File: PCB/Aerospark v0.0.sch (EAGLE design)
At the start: 15 parts, among them T1 2N3904

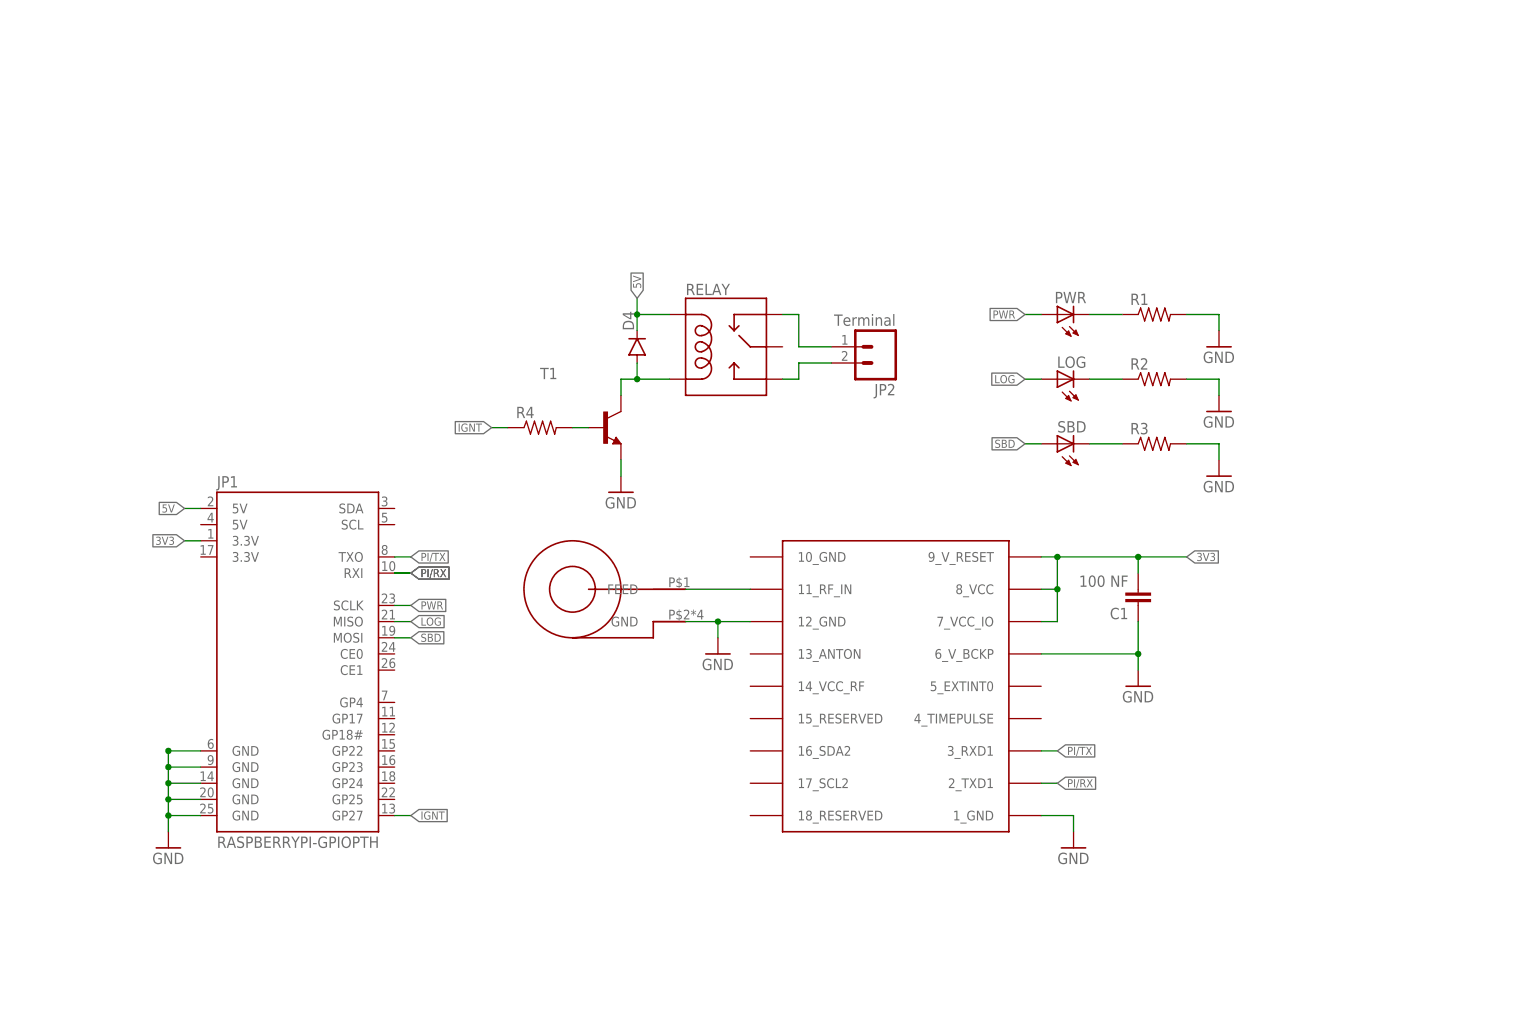
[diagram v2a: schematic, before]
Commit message: Updated PCB to optoisolator & darlington drivers
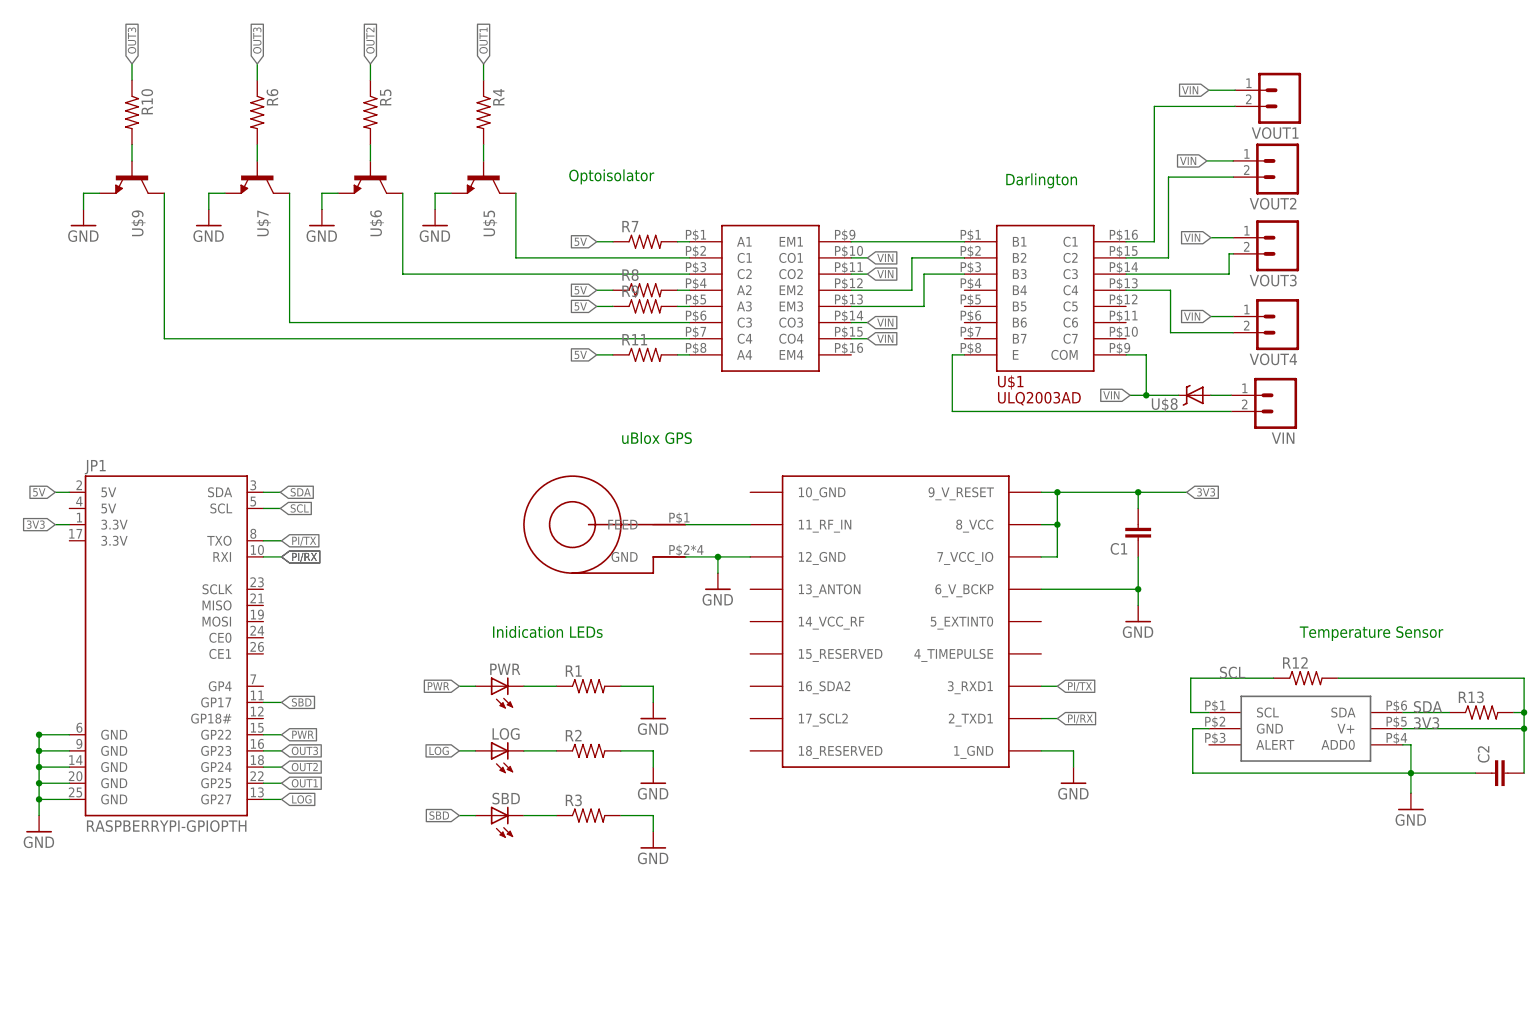
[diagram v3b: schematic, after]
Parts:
- removed D4: (no value), SparkFun-DiscreteSemi:DIODESMB
- removed JP2: Terminal, SparkFun-Connectors:M023.5MM_LOCK
- removed RELAY: RELAYPTH3, SparkFun-Electromechanical:RELAYPTH3
- removed T1: 2N3904, transistor:2N3904
- added C2: (no value), SparkFun-Capacitors:CAP0805
- added R10, R11, R12, R13, R5, R6, R7, R8, R9: (no value), resistor:R-US_R0805
- added U$1: ULQ2003A, ULQ2003AD:ULQ2003A
- added U$10: TMP102, TMP102:TMP102
- added U$4: ILQ2-X009, ILQ2-X009:ILQ2-X009
- added U$5, U$6, U$7, U$9: MMBT3904FSCT-ND, GuShH:MMBT3904FSCT-ND
- added U$8: VISHAY_SCHOTTKY, Ava:VISHAY_SCHOTTKY
- added VIN, VOUT1, VOUT2, VOUT3, VOUT4: M023.5MM_LOCK, SparkFun-Connectors:M023.5MM_LOCK
- C1: value 100 NF -> (none)
- R4: MF SLI (CML/IDI) -> (none); MPN CMD17-21VGD/TR8 -> (none); OC_NEWARK 34C8662 -> (none)
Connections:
- removed net IGNT: JP1.GP27, R4.1
- new net N$10: U$4.C1, U$5.C
- new net N$12: U$4.C2, U$6.C
- new net N$13: U$4.C3, U$7.C
- new net N$14: U$1.E, VIN.2
- new net N$15: R4.2, U$5.B
- new net N$16: R5.2, U$6.B
- new net N$17: R6.2, U$7.B
- new net N$18: U$8.A, VIN.1
- new net N$20: U$1.C2, VOUT2.2
- new net N$21: U$1.C3, VOUT3.2
- new net N$22: U$1.C4, VOUT4.2
- new net N$24: U$1.B1, U$4.EM1
- new net N$25: U$1.B2, U$4.EM2
- new net N$26: U$1.B3, U$4.EM3
- new net N$27: R10.2, U$9.B
- new net N$28: U$4.C4, U$9.C
- new net N$29: R11.2, U$4.A4
- new net OUT1: JP1.GP25, R4.1
- new net OUT2: JP1.GP24, R5.1
- new net OUT3: JP1.GP23, R10.1, R6.1
- new net SCL: JP1.SCL, R12.1, U$10.SCL
- new net SDA: JP1.SDA, R13.1, U$10.SDA
- new net VIN: U$1.COM, U$4.CO1, U$4.CO2, U$4.CO3, U$4.CO4, U$8.C, VOUT1.1, VOUT2.1, VOUT3.1, VOUT4.1
- net 3V3: now also C2.2, R12.2, R13.2, U$10.V+
- net 5V: now also R11.1, R7.1, R8.1, R9.1; no longer D4.C, RELAY.COIL1
- net GND: now also C2.1, U$10.ADD0, U$10.GND, U$5.E, U$6.E, U$7.E, U$9.E; no longer T1.E
- net LOG: now also JP1.GP27; no longer JP1.MISO
- net N$2: now also R7.2, U$4.A1; no longer JP2.1, RELAY.NC
- net N$6: now also R8.2, U$4.A2; no longer R4.2, T1.B
- net N$7: now also R9.2, U$4.A3; no longer JP2.2, RELAY.NO
- net N$8: now also U$1.C1, VOUT1.2; no longer D4.A, RELAY.COIL2, T1.C
- net PWR: now also JP1.GP22; no longer JP1.SCLK
- net SBD: now also JP1.GP17; no longer JP1.MOSI
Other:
- note added: "Darlington"
- note added: "Inidication LEDs"
- note added: "Optoisolator"
- note added: "Temperature Sensor"
- note added: "uBlox GPS"
- moved on the sheet: C1, JP1, LOG, PWR, R1, R2, R3, R4, SBD

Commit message: Updated PCB and added mounting hole
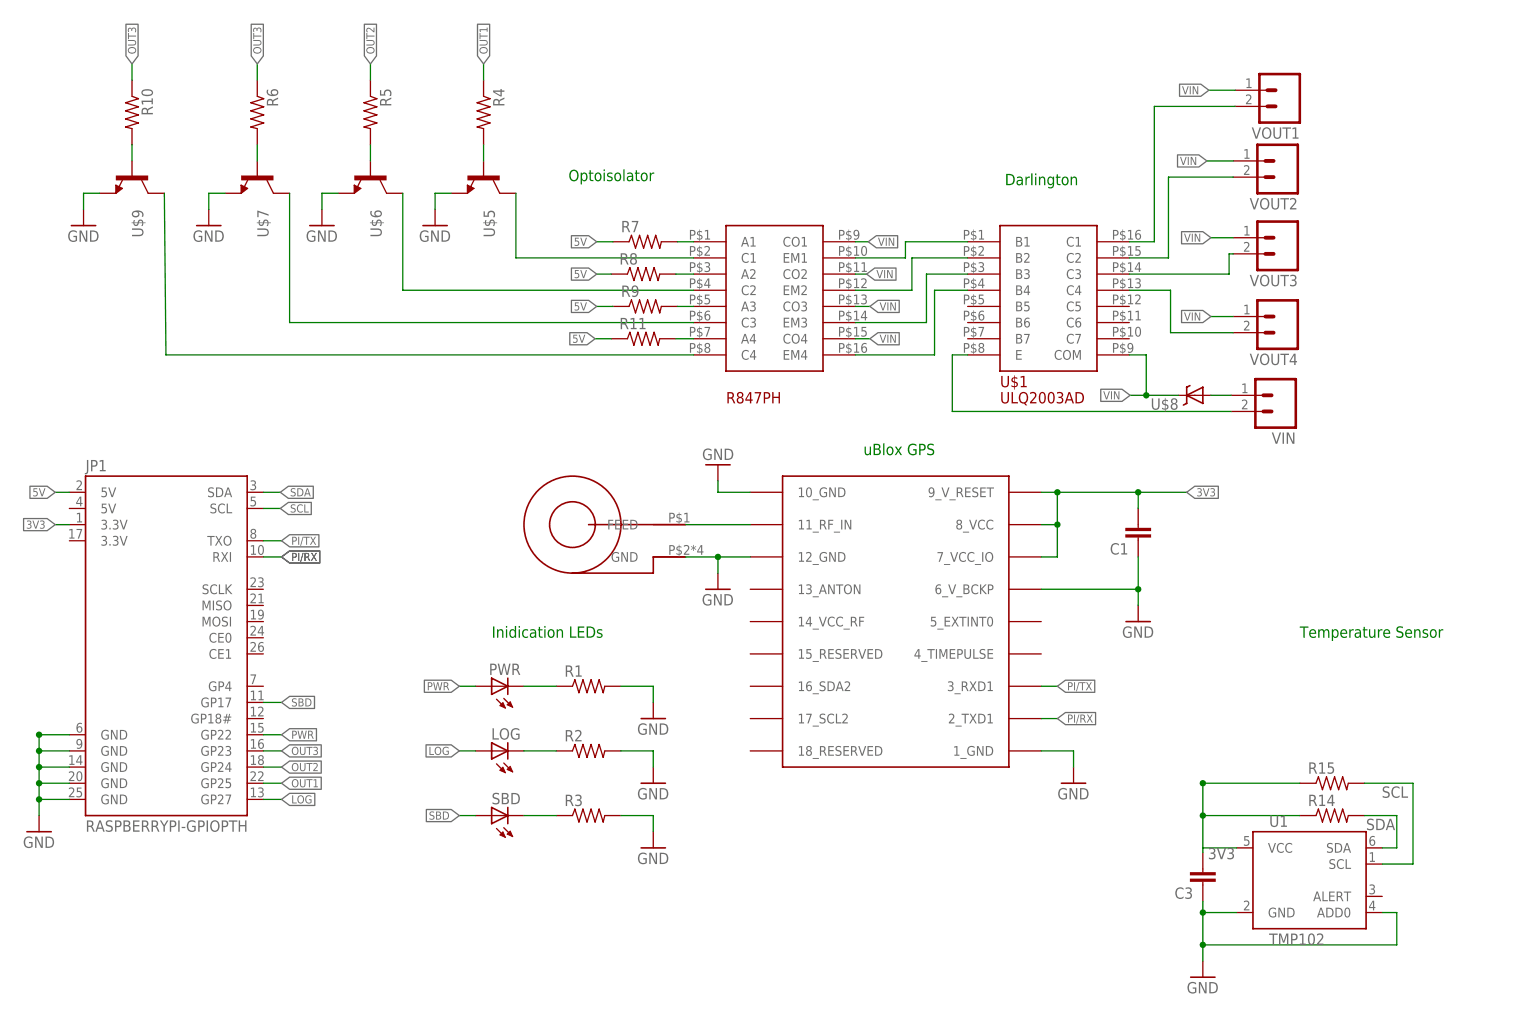
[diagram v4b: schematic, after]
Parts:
- removed C2: (no value), SparkFun-Capacitors:CAP0805
- removed R12, R13: (no value), resistor:R-US_R0805
- removed U$10: TMP102, TMP102:TMP102
- removed U$4: ILQ2-X009, ILQ2-X009:ILQ2-X009
- added C3: (no value), SparkFun-Capacitors:CAP0805
- added R14, R15: (no value), resistor:R-US_R0805
- added U$11: K847PH, K847PH:K847PHDIP16
- added U1: TMP102, SparkFun-Sensors:TMP102
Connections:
- removed net N$24: U$1.B1, U$4.EM1
- removed net N$26: U$1.B3, U$4.EM3
- new net N$11: U$1.B1, U$11.EM1
- new net N$23: U$1.B3, U$11.EM3
- new net N$30: U$1.B4, U$11.EM4
- net 3V3: now also C3.2, R14.1, R15.1, U1.VCC; no longer C2.2, R12.2, R13.2, U$10.V+
- net GND: now also C3.1, U$2.10_GND, U1.ADD0, U1.GND; no longer C2.1, U$10.ADD0, U$10.GND
- net N$10: now also U$11.C1; no longer U$4.C1
- net N$12: now also U$11.C2; no longer U$4.C2
- net N$13: now also U$11.C3; no longer U$4.C3
- net N$2: now also U$11.A1; no longer U$4.A1
- net N$25: now also U$11.EM2; no longer U$4.EM2
- net N$28: now also U$11.C4; no longer U$4.C4
- net N$29: now also U$11.A4; no longer U$4.A4
- net N$6: now also U$11.A2; no longer U$4.A2
- net N$7: now also U$11.A3; no longer U$4.A3
- net SCL: now also R15.2, U1.SCL; no longer R12.1, U$10.SCL
- net SDA: now also R14.2, U1.SDA; no longer R13.1, U$10.SDA
- net VIN: now also U$11.CO1, U$11.CO2, U$11.CO3, U$11.CO4; no longer U$4.CO1, U$4.CO2, U$4.CO3, U$4.CO4
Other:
- moved on the sheet: R11, R8, U$1

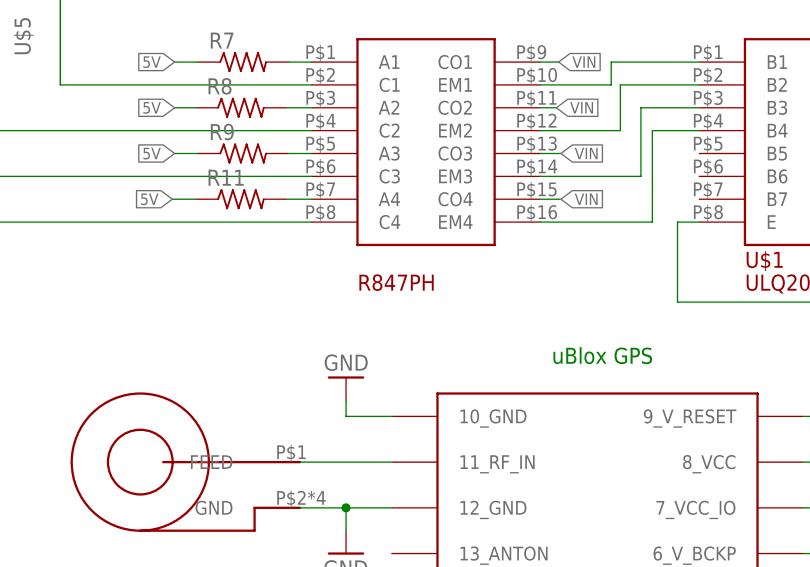
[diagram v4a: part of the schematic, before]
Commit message: Updated PCB and added mounting hole
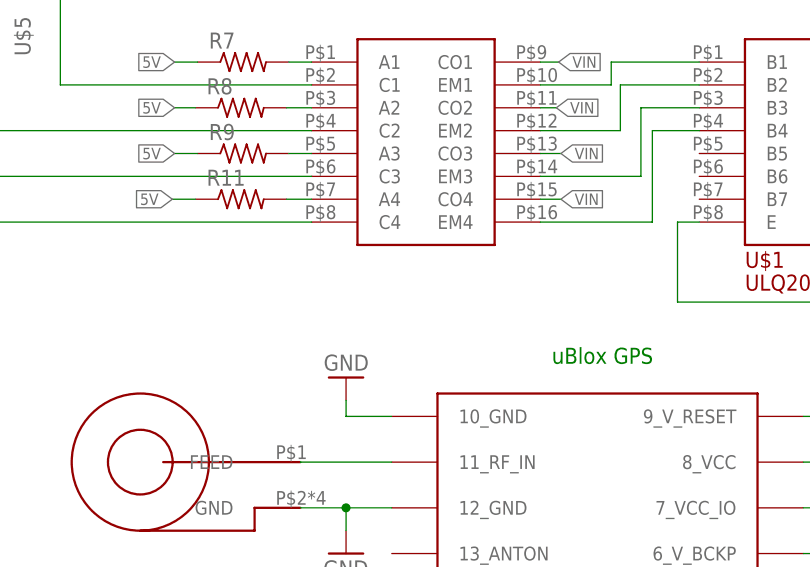
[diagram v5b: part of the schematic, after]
